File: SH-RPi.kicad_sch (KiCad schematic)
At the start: 0 parts

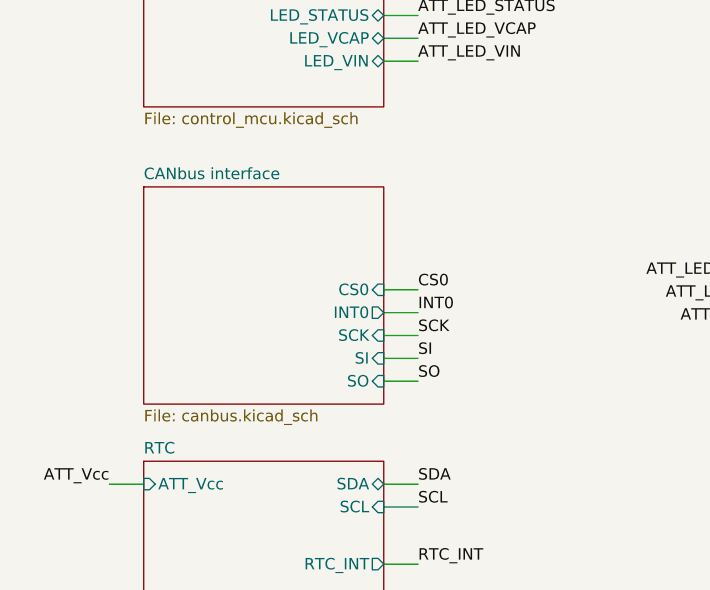
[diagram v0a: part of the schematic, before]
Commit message: Remove the CAN bus interface
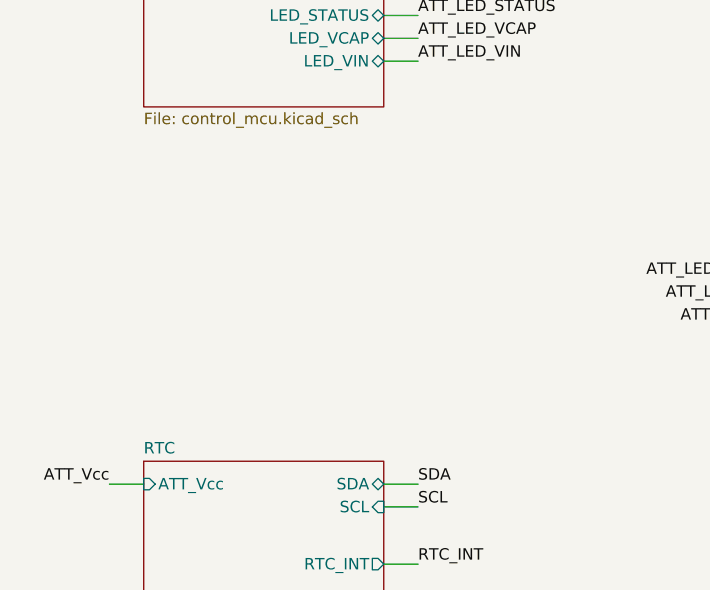
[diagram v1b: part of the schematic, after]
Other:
- removed sheet CANbus interface

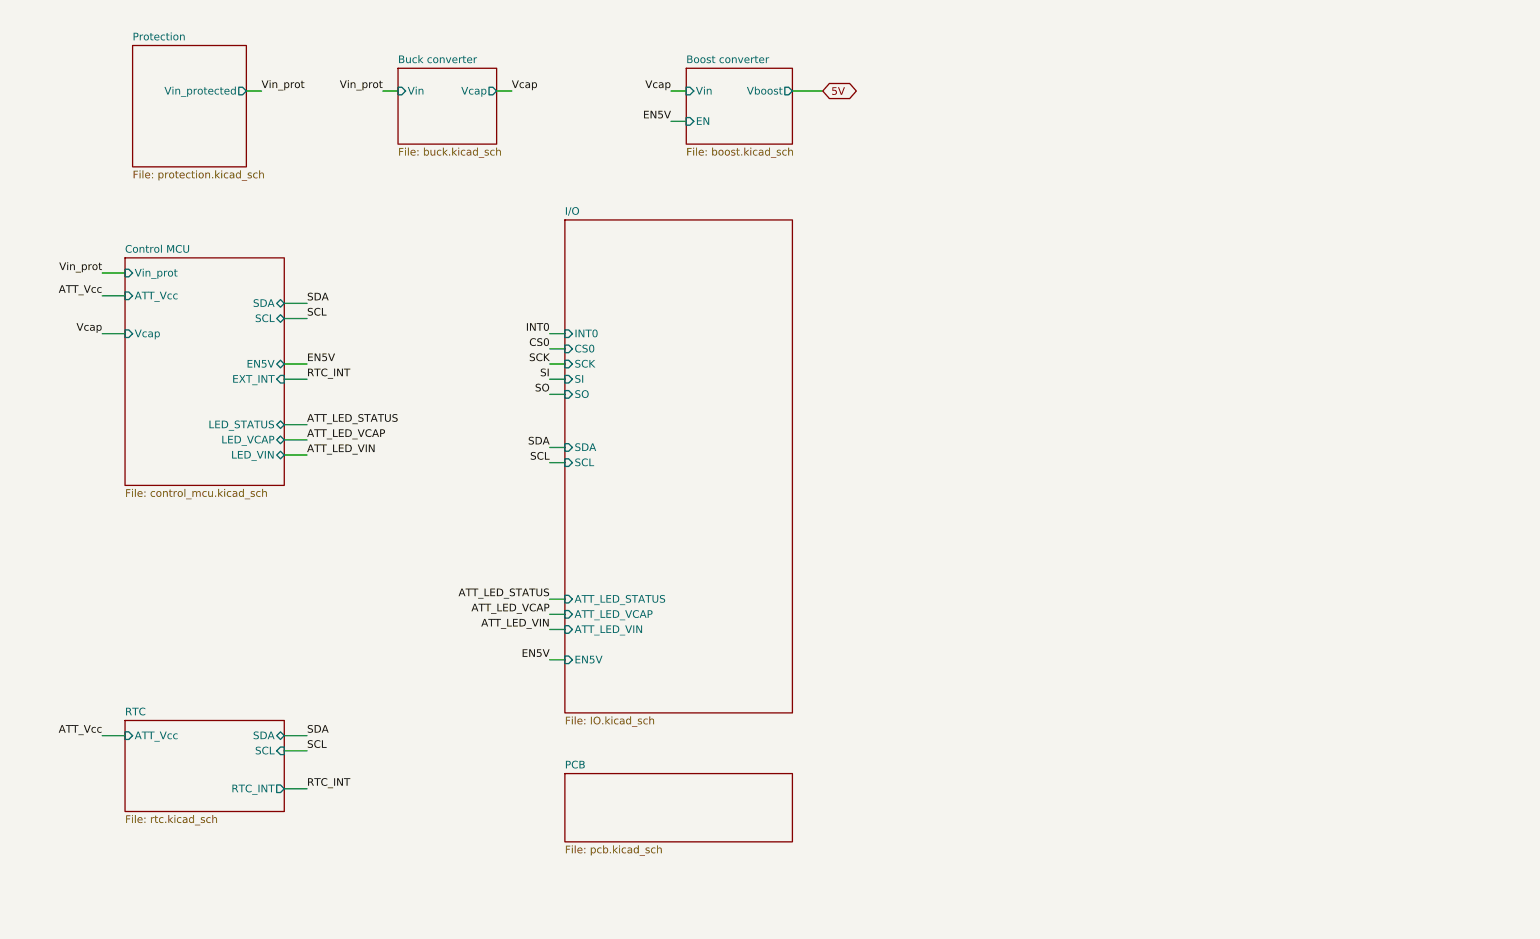
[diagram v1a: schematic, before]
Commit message: Change the power supply topology
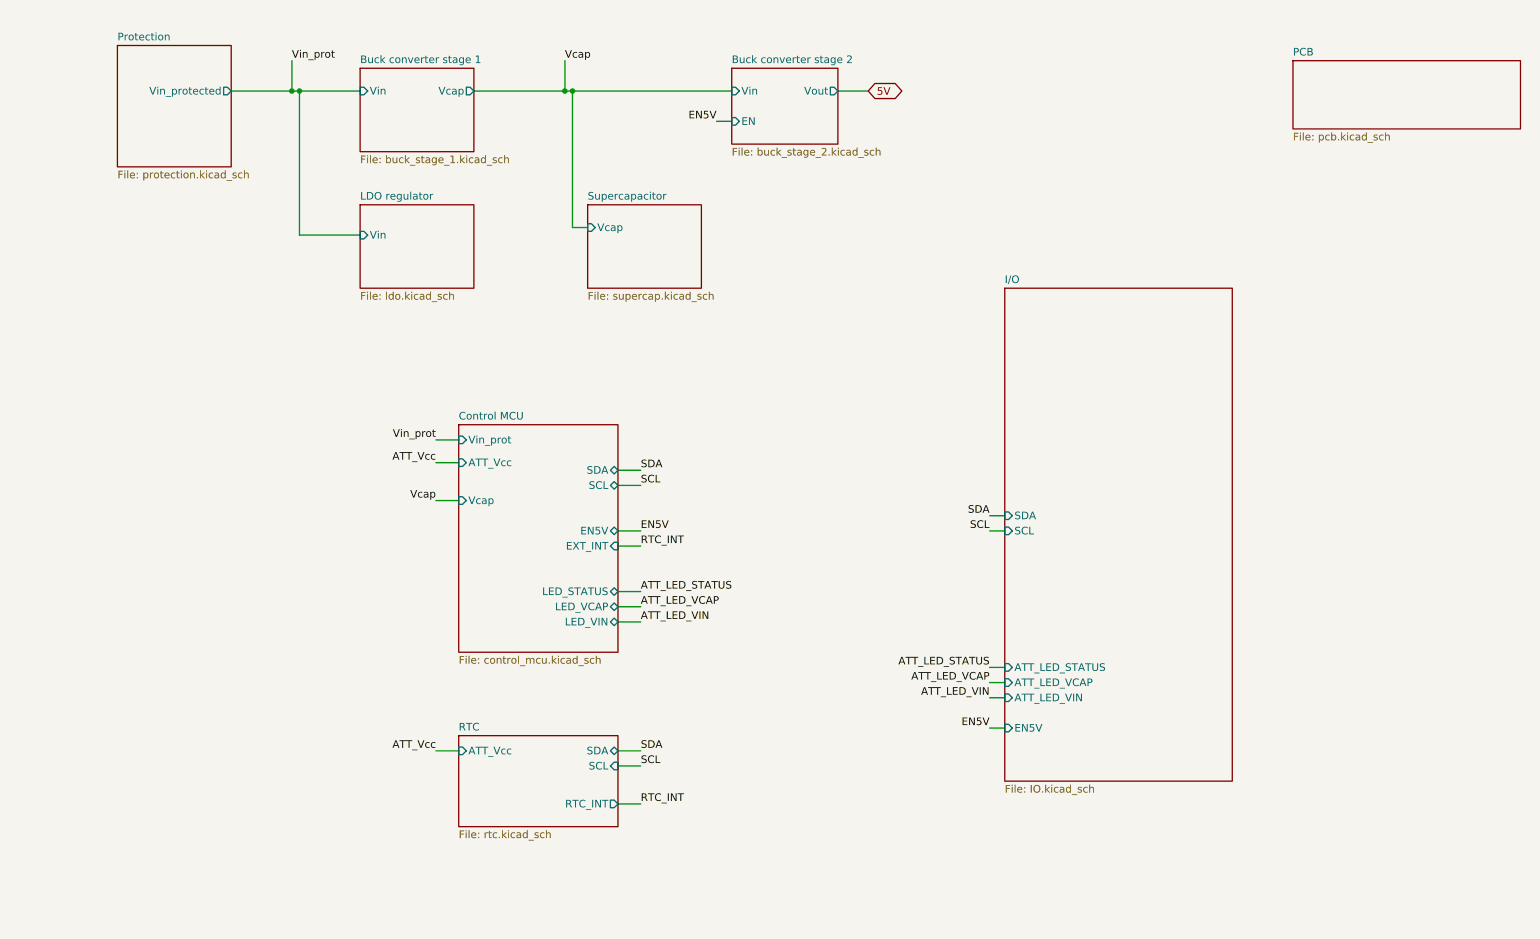
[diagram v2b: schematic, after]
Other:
- sheet Boost converter renamed Buck converter stage 2
- sheet Buck converter renamed Buck converter stage 1
- added sheet LDO regulator (ldo.kicad_sch)
- added sheet Supercapacitor (supercap.kicad_sch)
- sheet Buck converter stage 1: file buck.kicad_sch -> buck_stage_1.kicad_sch
- sheet Buck converter stage 2: file boost.kicad_sch -> buck_stage_2.kicad_sch
- sheet Buck converter stage 2 ports: added Vout; removed Vboost
- sheet I/O ports: added none; removed CS0, INT0, SCK, SI, SO

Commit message: SH-RPi v2 schematic design
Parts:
- added J101: Power input, symbol Connector_Generic:Conn_01x02
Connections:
- new net GND: J101.1 (Pin_1)
- new net Vin: J101.2 (Pin_2)
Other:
- sheet Buck converter stage 1 ports: added Iin, Vout; removed Vcap
- sheet Control MCU ports: added Iin, LED_1, LED_2, LED_3, LED_4, RTC_INT, RXD0, RXD5, TXD0, TXD5; removed ATT_Vcc, EXT_INT, LED_STATUS, LED_VCAP, LED_VIN
- sheet I/O ports: added LED_1, LED_2, LED_3, LED_4, RXD0, RXD5, TXD0, TXD5; removed ATT_LED_STATUS, ATT_LED_VCAP, ATT_LED_VIN, EN5V
- sheet LDO regulator ports: added HS_Vin, LS_Vin; removed Vin
- sheet Protection ports: added Vin; removed none
- sheet RTC ports: added none; removed ATT_Vcc
- note added: "3 * 3.0V supercaps and balancing circuit"
- note added: "5-9.0V 0-5V at startup"
- note added: "9-32V"
- note added: "Drop input to 5V"
- note added: "Drop input to 9.0V Limit input current to 0.8A"
- note added: "Fuse TVS Reverse polarity prot. Reverse current prot. EMI filtering"
- note added: "Power for the 3.3V rail"
- note added: "TODO: - Adjustable input current limit"

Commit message: WIP: Assign footprints and LCSC part numbers
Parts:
- J101: footprint (none) -> Connector_Phoenix_MC:PhoenixContact_MC_1,5_2-G-3.81_1x02_P3.81mm_Horizontal; LCSC (none) -> C8387

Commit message: Assign footprints and part numbers to components
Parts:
- J101: value Power input -> Conn_01x02
